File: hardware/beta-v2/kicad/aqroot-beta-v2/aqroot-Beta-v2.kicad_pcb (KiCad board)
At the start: 6 copper layers, 72 x 148 mm, 324 parts, among them J1 FH69-50S-0.5SH, J2 Molex_5025700893, J3 USB_C_Receptacle_USB2.0_16P, J4 JST-PH-2 BATTERY, J5 COMMUNITY_PORT_1x24, J6 JST-PH-2 SPEAKER, J7 BM02B-ACHSS-GAN-ETF, J8 QWIIC_STEMMA_QT, Q1 AO3400A, Q10 2N7002, Q2 NTMD4820N, Q3 NTMD4820N, Q4 BSS138, Q5 AO3401A, Q6 BSS138, Q7 BSS138, Q8 BSS138, Q9 BSS138, SW1 BOOT, SW2 UP, SW3 DOWN, SW4 LEFT, SW5 RIGHT, SW6 A_SELECT, SW7 B_BACK, SW9 SW_SPDT, U1 ESP32-S3-WROOM-1, U10 USBLC6-2SC6, U11 BQ25185, U12 TPS63020, U13 TPS61023, U14 MAX17048, U16 TCA4307DGKR, U17 TPS61169DCKR, U18 LTC4368-1, U19 TLV7032, U2 PCAL9535APW, U20 TPS22950C, U21 TPS61023, U22 TPS22950C, U23 PCAL9535APW, U3 PCAL9535APW, U4 BMI270, U5 MAX98357A, U6 TSOP38238, U7 E07-400M10S, U8 E22-900M22S, U9 ST25R3916-AQET, Y1 27.12MHz 10pF 3225-4P

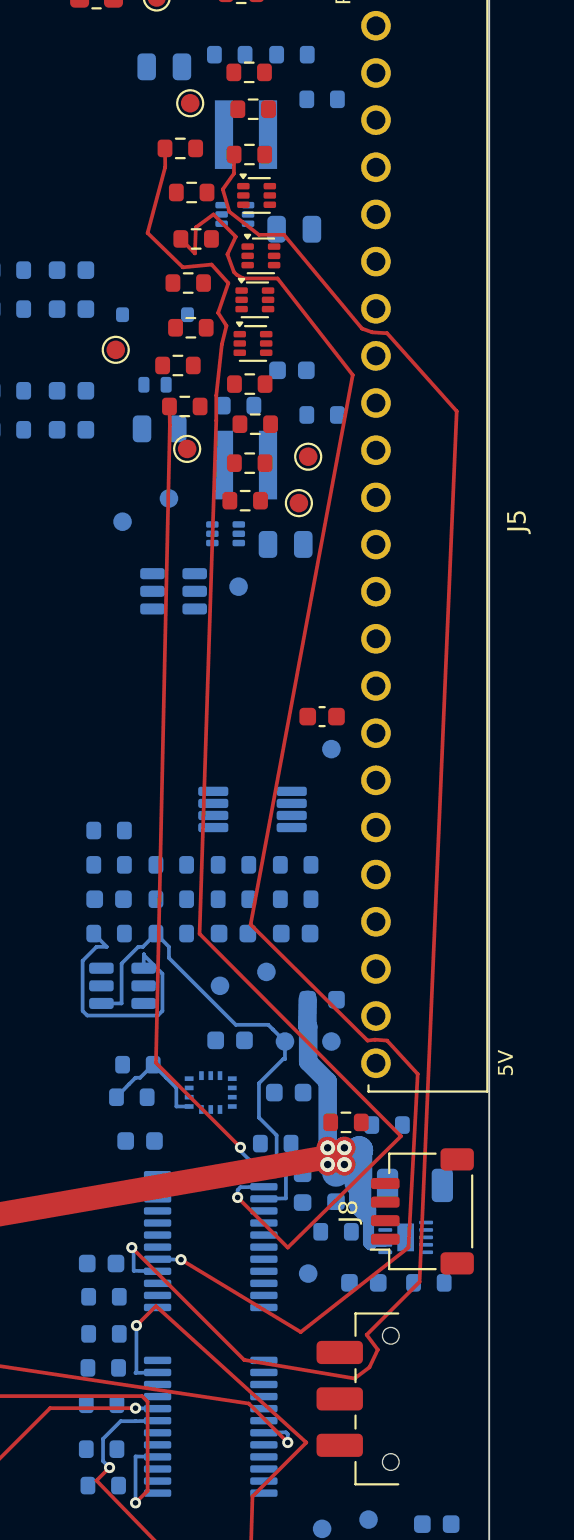
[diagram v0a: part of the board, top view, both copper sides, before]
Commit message: FBV2-P2-018: D-316 TWELFTH REST-OF-BOARD INCREMENTAL INCREMENT ROUTED + PROMOTED (a SINGLE west XGPIO net XGPIO3 at the 0.200 mm Default clearance) — the D-315 positive lead realised: one west haul keeps the D-269 0.300 mm floor to BAT_PROTECTED_P by geometry (haul->BPP 0.4739 mm), ZERO router-logic change
XGPIO3 (R54.1 F.Cu -> U3.7 B.Cu), the fifth XGPIO0..9 bank member, routed at the
0.200 mm Default clearance (NOT the 0.300 mm blanket the D-313/D-314 pilot PAIRS
used) and promoted. D-315 characterised the XGPIO2+XGPIO3 PAIR as a corridor-
capacity wall (both orders NO_FAR_RUN) and produced this positive lead: a single
west net routes clean at 0.200 mm and keeps D-269 by geometry (the west haul
clears BPP by >=0.47 mm; the real D-269-aware KiCad DRC arbitrates). Not rule
weakening; the 0.300 mm blanket was over-conservative for west members.

WIP RECOVERY (gitignored scratch only, ZERO routing-logic change): w/screen_018.py
had stalled before persisting evidence because it imported haul_bpp_min/BPP from
w/xgpio23_pair200_017.py, whose full XGPIO2+XGPIO3 PAIR driver runs at module
level -> the import re-routed the D-315 wall every load (cross-module recurrence
of the D-314 module-level-driver bug). Fix = drop the import, inline the self-
contained helper, screen only /XGPIO3; one managed foreground process completed
and persisted the evidence.

route->gate->promote (real full-board D-286 gate): promoted
sha 95bc07be.. -> d730c74d186ebcc7d2f0aa513776778ce1cb9c9659029a2fffd5e2261e3ac97d;
tracks 669->691 (+22); vias 66->67 (+1); ratsnest 677->676 (-1); journal 104->105
(+1 REST_INC); only In1/In4 re-poured; real DRC identical (clearance 0).

Tests: new G29; G18-G28 auto-generalise; router_regression ALL PASS G1-G29 twice
(deterministic); new incremental_probe_017.py PASS; _006..016 + phaseB_bringup_
probe_005 (691/67/105; 20 routed rest nets, 144 unrouted) PASS; live_fingerprint
bumped once; independent kicad-cli DRC confirms clearance 0; D-269/D-264/DRU
board-swap A/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
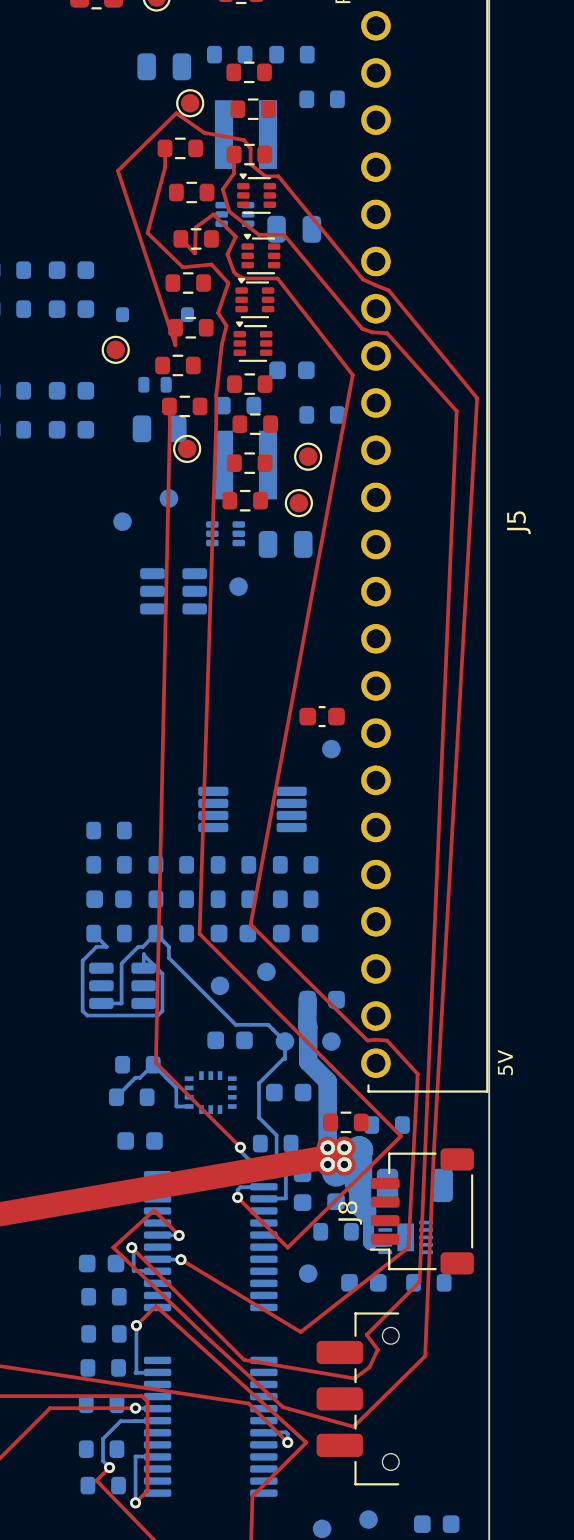
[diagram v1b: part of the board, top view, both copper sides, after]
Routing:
- net /XGPIO3: track 0.00 -> 118.3 mm, vias 0 -> 1
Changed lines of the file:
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@@
+	)
+	(segment
+		(start 55.105848 28.80428)
+		(end 55.1 29.75)
+		(width 0.2)
+		(layer "F.Cu")
+		(net "/XGPIO3")
+	)
+	(segment
+		(start 56.65 18.3)
+		(end 58.8 18.7)
+		(width 0.2)
+		(layer "F.Cu")
+		(net "/XGPIO3")
+	)
+	(segment
+		(start 52 20.35)
+		(end 55.15 17.25)
+		(width 0.2)
+		(layer "F.Cu")
+		(net "/XGPIO3")
+	)
+	(segment
+		(start 53.95 76.35)
+		(end 55.3 77.7)
+		(width 0.2)
+		(layer "F.Cu")
+		(net "/XGPIO3")
+	)
+	(segment
+		(start 59.15 19.15)
+		(end 59.15 20)
+		(width 0.2)
+		(layer "F.Cu")
+		(net "/XGPIO3")
+	)
+	(segment
+		(start 68.55 84.2)
+		(end 64.7 88)
+		(width 0.2)
+		(layer "F.Cu")
+		(net "/XGPIO3")
+	)
+	(segment
+		(start 71.35 32.6)
+		(end 69 73.55)
+		(width 0.2)
+		(layer "F.Cu")
+		(net "/XGPIO3")
+	)
+	(segment
+		(start 51.75 78.35)
+		(end 53.95 76.35)
+		(width 0.2)
+		(layer "F.Cu")
+		(net "/XGPIO3")
+	)
+	(segment
+		(start 56.7 83.1)
+		(end 51.75 78.35)
+		(width 0.2)
+		(layer "F.Cu")
+		(net "/XGPIO3")
+	)
+	(segment
+		(start 60.65 20.65)
+		(end 65.2 26.2)
+		(width 0.2)
+		(layer "F.Cu")
+		(net "/XGPIO3")
+	)
+	(segment
+		(start 69 73.55)
+		(end 68.55 84.2)
+		(width 0.2)
+		(layer "F.Cu")
+		(net "/XGPIO3")
+	)
+	(segment
+		(start 60.9 86.95)
+		(end 56.7 83.1)
+		(width 0.2)
+		(layer "F.Cu")
+		(net "/XGPIO3")
+	)
+	(segment
+		(start 64.7 88)
+		(end 60.9 86.95)
+		(width 0.2)
+		(layer "F.Cu")
+		(net "/XGPIO3")
+	)
+	(segment
+		(start 66.6 26.8)
+		(end 71.35 32.6)
+		(width 0.2)
+		(layer "F.Cu")
+		(net "/XGPIO3")
+	)
+	(segment
+		(start 58.8 18.7)
+		(end 59.15 19.15)
+		(width 0.2)
+		(layer "F.Cu")
+		(net "/XGPIO3")
+	)
+	(segment
+		(start 65.2 26.2)
+		(end 65.85 26.5)
+		(width 0.2)
+		(layer "F.Cu")
+		(net "/XGPIO3")
+	)
+	(segment
+		(start 59.15 20)
+		(end 59.95 20.65)
+		(width 0.2)
+		(layer "F.Cu")
+		(net "/XGPIO3")
+	)
+	(segment
+		(start 59.95 20.65)
+		(end 60.65 20.65)
+		(width 0.2)
+		(layer "F.Cu")
+		(net "/XGPIO3")
+	)
+	(segment
+		(start 55.1 29.75)
+		(end 52 20.35)
+		(width 0.2)
+		(layer "F.Cu")
+		(net "/XGPIO3")
+	)
+	(segment
+		(start 65.85 26.5)
+		(end 66.6 26.8)
+		(width 0.2)
+		(layer "F.Cu")
+		(net "/XGPIO3")
+	)
+	(segment
+		(start 55.15 17.25)
+		(end 56.65 18.3)
+		(width 0.2)
+		(layer "F.Cu")
+		(net "/XGPIO3")
+	)
+	(via
+		(at 55.3 77.7)
+		(size 0.6)
+		(drill 0.3)
+		(layers "F.Cu" "B.Cu")
+		(net "/XGPIO3")
+	)
+	(segment
+		(start 54.1375 77.675)
+		(end 55.3 77.7)
+		(width 0.2)
+		(layer "B.Cu")
+		(net "/XGPIO3")
 	)
 	(segment

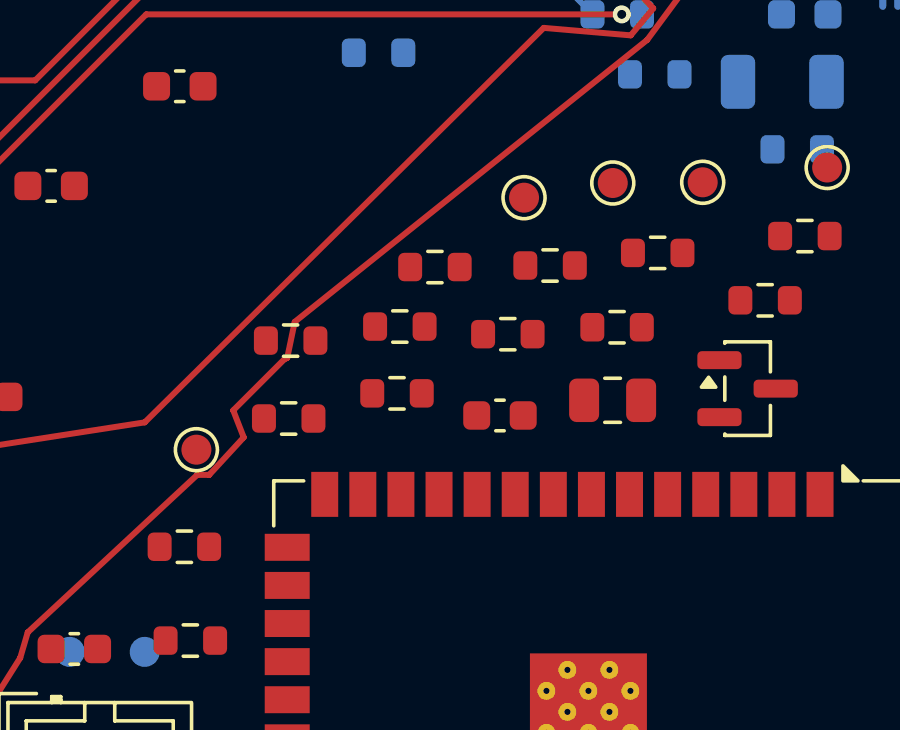
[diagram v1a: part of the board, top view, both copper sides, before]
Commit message: FBV2-P2-020: D-318 THIRTEENTH REST-OF-BOARD INCREMENTAL INCREMENT ROUTED + PROMOTED — the IMU/I2C-local interrupt strap BMI270_INT1_STRAP (R18.2/R110.1/TP3.1 F.Cu -> U1.15 MCU GPIO), a 4-pad multi-terminal ALL-F.Cu SAME-LAYER MST with NO via (the cleanest class), the FIRST clean increment OUTSIDE the saturated west-XGPIO F.Cu corridor (the D-317 mandate); a governed CTO ACCEPT + PROMOTE, ZERO router-logic change; stale CURRENT_STATE §5 (FBV2-P2-018) repaired to the D-317 truth
Evidence-first: repaired the stale CURRENT_STATE §5, then a read-only screen
(w/screen_020.py) measured all 144 unrouted rest nets (44 ALLOW / 100 EXCL;
rejected west/east XGPIO corridor, RF/NFC/radio incl. 04_SPI_B, USB, shared bus
data/clocks, switching/boost/class-D, community-header mass, U11_PROG, PWR_SENSE,
rails). Selected BMI270_INT1_STRAP (the mandate's welcomed IMU/I2C-local
category); all four pads on F.Cu -> three same-layer F.Cu MST runs, NO via.
Route ALL OK (18 F.Cu seg, 0 via); real full-board gate (D-286) PASS every check
(0 Phase-A altered, 18 new items all target-net, 0 zones fill-changed, net
open_edges 3->0, ratsnest 676->673 -3, no new/worse DRC, unconnected 499->499).

Promoted: sha256 d730c74d... -> 78bf82da537a22697a860c23822599246e0534a8c4c311e12bc3d5b857a28816
tracks 691->709 (+18), vias 67 (unchanged, no via), 6 layers / 41 zones,
ratsnest 676->673 (-3), journal 105->108 (+3 REST_INC).

Tests: new G30; router_regression ALL PASS G1-G30 twice (deterministic); new
incremental_probe_018.py PASS; _006..017 + phaseB_bringup_probe_005 (709/67/108;
21 routed rest nets, 143 unrouted) PASS; live_fingerprint bumped once; independent
kicad-cli DRC matches (clearance 0, 0 schematic-parity); D-269/D-264/DRU board-swap
A/B (committed D-316 vs promoted D-318) verdicts IDENTICAL (pre-existing
synthetic/intrinsic flakes, not regressions). Open owner decisions: NONE.
NEXT FBV2-P2-021: next clean rest-of-board increment in an open region.

Co-Authored-By: Claude Opus 4.8 (1M context) 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
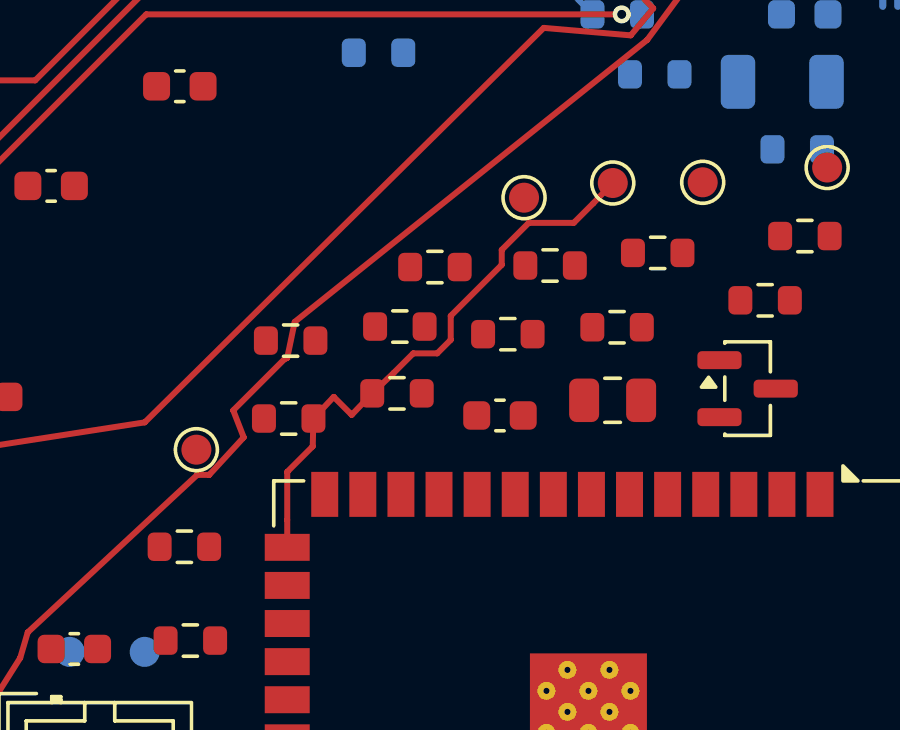
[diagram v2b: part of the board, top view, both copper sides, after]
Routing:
- net /BMI270_INT1_STRAP: track 0.00 -> 19.2 mm
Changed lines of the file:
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@@
+	)
+	(segment
+		(start 49.45 114.55)
+		(end 50.25 114.55)
+		(width 0.2)
+		(layer "F.Cu")
+		(net "/BMI270_INT1_STRAP")
+	)
+	(segment
+		(start 56.101523 108.870898)
+		(end 55.45 109.55)
+		(width 0.2)
+		(layer "F.Cu")
+		(net "/BMI270_INT1_STRAP")
+	)
+	(segment
+		(start 53.3 110.2)
+		(end 54.8 110.2)
+		(width 0.2)
+		(layer "F.Cu")
+		(net "/BMI270_INT1_STRAP")
+	)
+	(segment
+		(start 50.25 114.55)
+		(end 50.7 114.1)
+		(width 0.2)
+		(layer "F.Cu")
+		(net "/BMI270_INT1_STRAP")
+	)
+	(segment
+		(start 52.4 111.1)
+		(end 53.3 110.2)
+		(width 0.2)
+		(layer "F.Cu")
+		(net "/BMI270_INT1_STRAP")
+	)
+	(segment
+		(start 47.4 116.6)
+		(end 46.8 116)
+		(width 0.2)
+		(layer "F.Cu")
+		(net "/BMI270_INT1_STRAP")
+	)
+	(segment
+		(start 45.25 121.015)
+		(end 45.25 120.1)
+		(width 0.2)
+		(layer "F.Cu")
+		(net "/BMI270_INT1_STRAP")
+	)
+	(segment
+		(start 46.1 117.65)
+		(end 45.25 118.5)
+		(width 0.2)
+		(layer "F.Cu")
+		(net "/BMI270_INT1_STRAP")
+	)
+	(segment
+		(start 50.7 114.1)
+		(end 50.7 113.3)
+		(width 0.2)
+		(layer "F.Cu")
+		(net "/BMI270_INT1_STRAP")
+	)
+	(segment
+		(start 48.8 115.2)
+		(end 49.45 114.55)
+		(width 0.2)
+		(layer "F.Cu")
+		(net "/BMI270_INT1_STRAP")
+	)
+	(segment
+		(start 48.083956 115.882411)
+		(end 48.8 115.2)
+		(width 0.2)
+		(layer "F.Cu")
+		(net "/BMI270_INT1_STRAP")
+	)
+	(segment
+		(start 50.7 113.3)
+		(end 52.4 111.6)
+		(width 0.2)
+		(layer "F.Cu")
+		(net "/BMI270_INT1_STRAP")
+	)
+	(segment
+		(start 54.8 110.2)
+		(end 55.45 109.55)
+		(width 0.2)
+		(layer "F.Cu")
+		(net "/BMI270_INT1_STRAP")
+	)
+	(segment
+		(start 46.123856 116.721301)
+		(end 46.8 116)
+		(width 0.2)
+		(layer "F.Cu")
+		(net "/BMI270_INT1_STRAP")
+	)
+	(segment
+		(start 48.083956 115.882411)
+		(end 47.4 116.6)
+		(width 0.2)
+		(layer "F.Cu")
+		(net "/BMI270_INT1_STRAP")
+	)
+	(segment
+		(start 45.25 118.5)
+		(end 45.25 120.1)
+		(width 0.2)
+		(layer "F.Cu")
+		(net "/BMI270_INT1_STRAP")
+	)
+	(segment
+		(start 52.4 111.6)
+		(end 52.4 111.1)
+		(width 0.2)
+		(layer "F.Cu")
+		(net "/BMI270_INT1_STRAP")
+	)
+	(segment
+		(start 46.123856 116.721301)
+		(end 46.1 117.65)
+		(width 0.2)
+		(layer "F.Cu")
+		(net "/BMI270_INT1_STRAP")
 	)
 	(segment

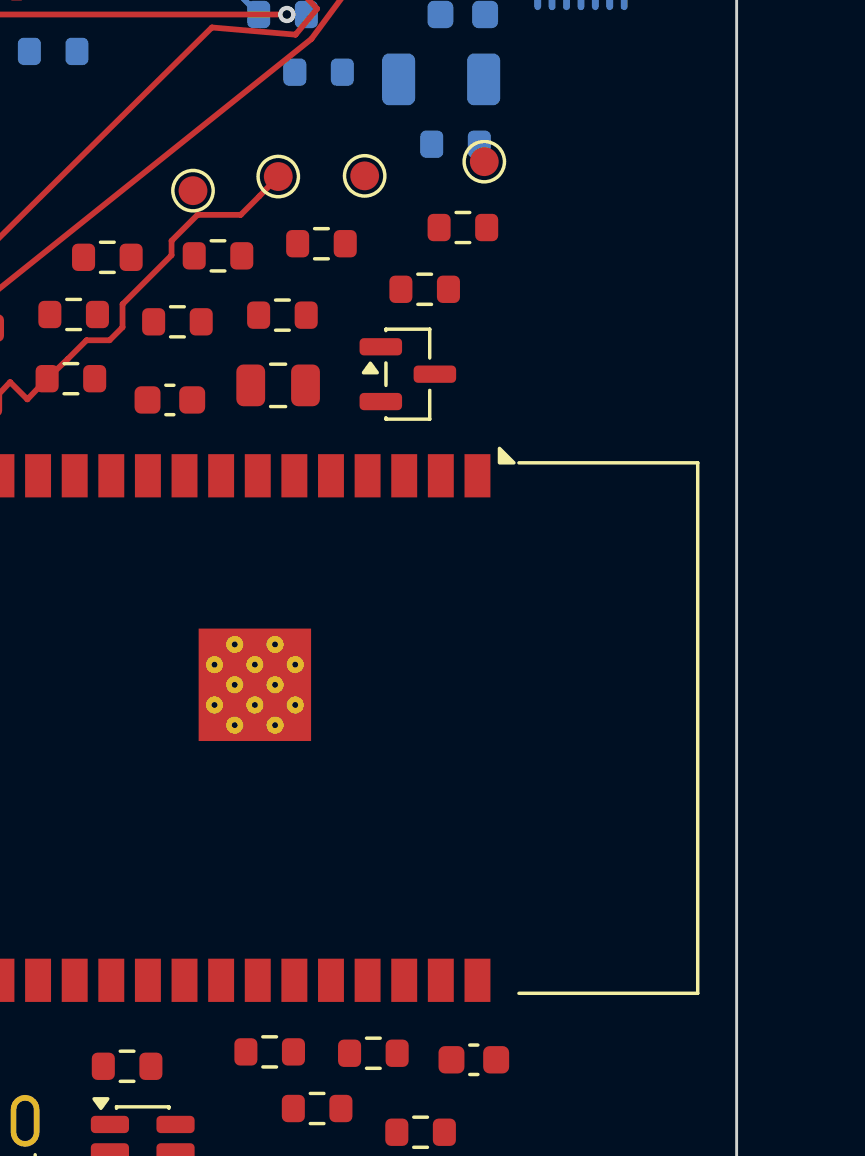
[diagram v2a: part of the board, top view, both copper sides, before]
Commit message: FBV2-P2-021: D-319 FOURTEENTH REST-OF-BOARD INCREMENTAL INCREMENT ROUTED + PROMOTED — the debug-console UART transmit line UART0_TXD_DBG (U1.37 ESP32 MCU -> TP35.1 test point), a dedicated 2-pad point-to-point net, SAME-LAYER F.Cu MST with NO via, a clean increment in an OPEN region 31.3 mm clear of BAT_PROTECTED_P (zero D-269 involvement); a governed CTO ACCEPT + PROMOTE, ZERO router-logic change
Selected on measured merit over the vetted alternates: w/screen_020.py screened all 143
unrouted rest nets (43 ALLOW / 100 EXCL; auto-classifier trap re-confirmed — converter-switching
Net-(L1/U12/U13-*)/BL_SW/BQ25185_SYS and USB-C connector Net-(J3-*) auto-ALLOW nets rejected on
role), then w/vet_021.py measured the clean functional shortlist. UART0_TXD_DBG is the best
coherent low-risk increment (simplest topology: 2-pad, 1 MST edge, all F.Cu -> NO via, no plane
re-pour; lowest congestion 9; 31.3 mm clear of BPP). The vetted BQ25185_STAT1/STAT2 pair was
measured NOT low-risk (STAT2 0.024 mm from BAT_PROTECTED_P through the U11/BQ25185 power-tree wall)
and rejected under "do not force a pair across a characterized power-tree wall".

Route ALL OK (31.755 mm F.Cu, 7 seg, 0 via). Gate PASS every check (real full-board D-286:
0 Phase-A altered, 7 new items all target-net, 0 zones fill-changed, net open_edges 1->0, 0 prior
pairs regressed, ratsnest 673->672 -1, no new/worse DRC, unconnected 499->499). Promoted:
sha 78bf82da... -> 57dcc8affb6c0f85f747fba025463b9cf0897c6712709692151020f56fdb8adf; tracks
709->716 (+7); vias 67 unchanged; 6 layers / 41 zones; ratsnest 673->672; journal 108->109.

Tests: new G31 (both pads connected, 7 trk 0.200 F.Cu 0 vias, ADD-ONLY); router_regression ALL
PASS G1-G31 twice (deterministic); new incremental_probe_019.py PASS; _006..018 + phaseB_005
(716/67/109; 22 routed rest, 142 unrouted) PASS; live_fingerprint bumped once; incremental_baseline_006.json
left stale-by-design (reverted); independent kicad-cli DRC clearance 0; D-269/D-264/DRU board-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
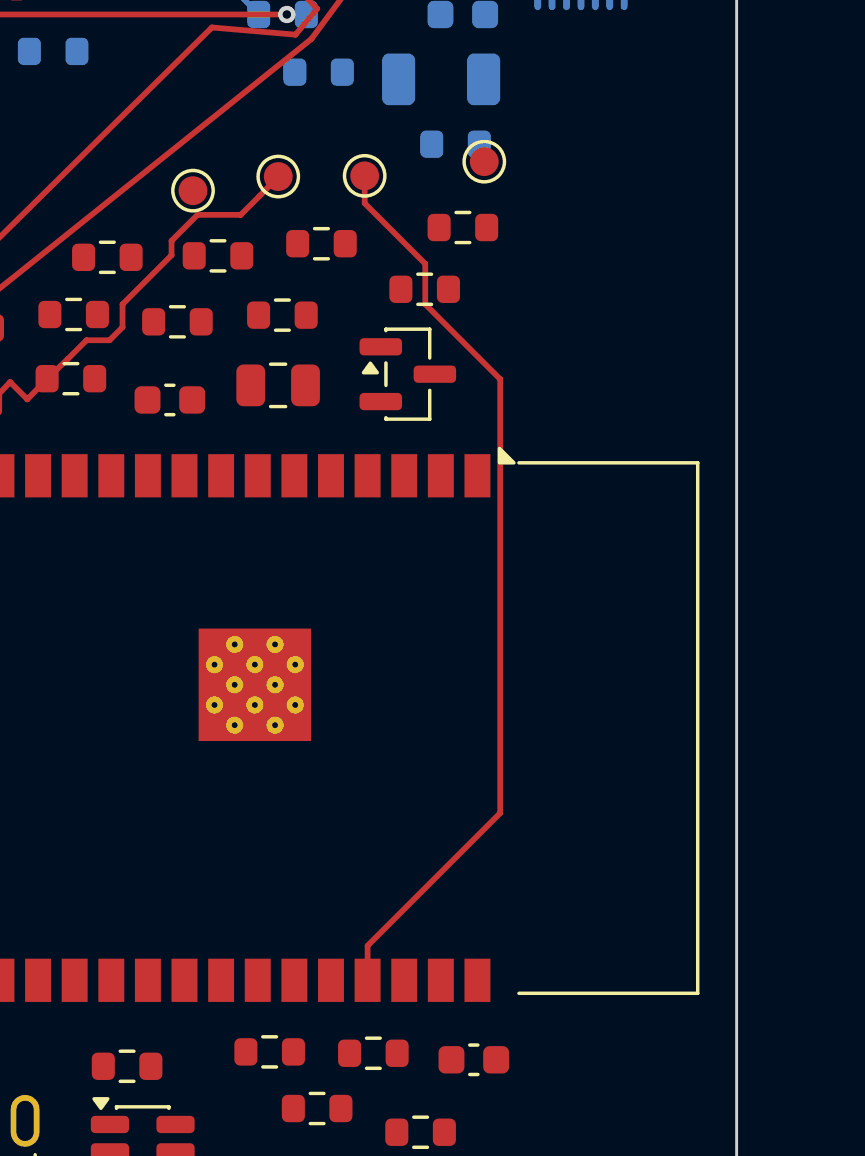
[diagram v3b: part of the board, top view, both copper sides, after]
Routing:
- net /02_MCU_CORE/UART0_TXD_DBG: track 0.00 -> 31.8 mm
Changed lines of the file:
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@@
+	)
+	(segment
+		(start 61.2 113.3)
+		(end 63.8 115.9)
+		(width 0.2)
+		(layer "F.Cu")
+		(net "/02_MCU_CORE/UART0_TXD_DBG")
+	)
+	(segment
+		(start 59.099302 108.84747)
+		(end 59.1 109.8)
+		(width 0.2)
+		(layer "F.Cu")
+		(net "/02_MCU_CORE/UART0_TXD_DBG")
+	)
+	(segment
+		(start 63.8 130.95)
+		(end 59.2 135.55)
+		(width 0.2)
+		(layer "F.Cu")
+		(net "/02_MCU_CORE/UART0_TXD_DBG")
+	)
+	(segment
+		(start 63.8 115.9)
+		(end 63.8 130.95)
+		(width 0.2)
+		(layer "F.Cu")
+		(net "/02_MCU_CORE/UART0_TXD_DBG")
+	)
+	(segment
+		(start 59.2 136.75)
+		(end 59.2 135.55)
+		(width 0.2)
+		(layer "F.Cu")
+		(net "/02_MCU_CORE/UART0_TXD_DBG")
+	)
+	(segment
+		(start 59.1 109.8)
+		(end 61.2 111.9)
+		(width 0.2)
+		(layer "F.Cu")
+		(net "/02_MCU_CORE/UART0_TXD_DBG")
+	)
+	(segment
+		(start 61.2 111.9)
+		(end 61.2 113.3)
+		(width 0.2)
+		(layer "F.Cu")
+		(net "/02_MCU_CORE/UART0_TXD_DBG")
 	)
 	(segment
